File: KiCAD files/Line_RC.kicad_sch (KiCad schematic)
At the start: 56 parts, among them IC1 ESP32-WROVER-E-N4R8, IC2 CP2102N-A02-GQFN28R, IC3 BC847BDW1T1G, IC4 TLV75533PDBVR, IC5 ST1S40IPHR, J1 XT60PW-M, J2 XT60PW-M, J3 Conn_02x02_Odd_Even, J6 Motor OUT, J7 Motor OUT, U1 SL19-121, U3 DRV8213RTER, U4 DRV8213RTER

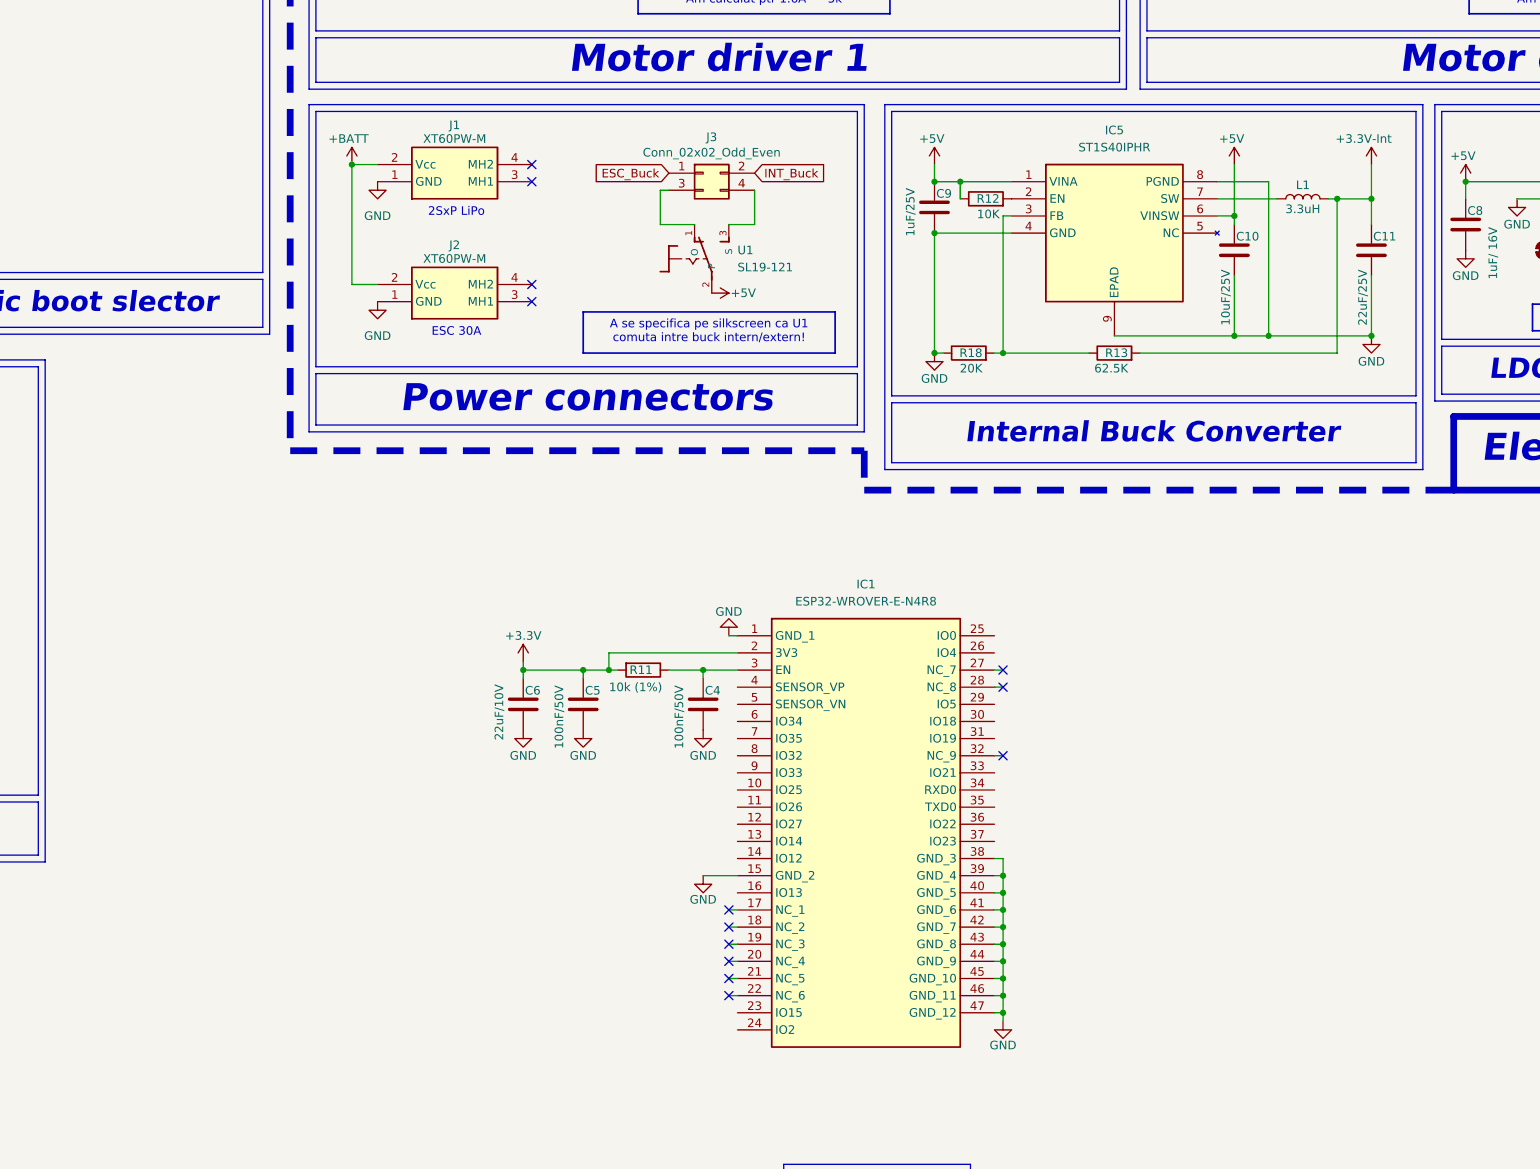
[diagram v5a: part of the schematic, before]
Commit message: Added the connector for the ribbon cable
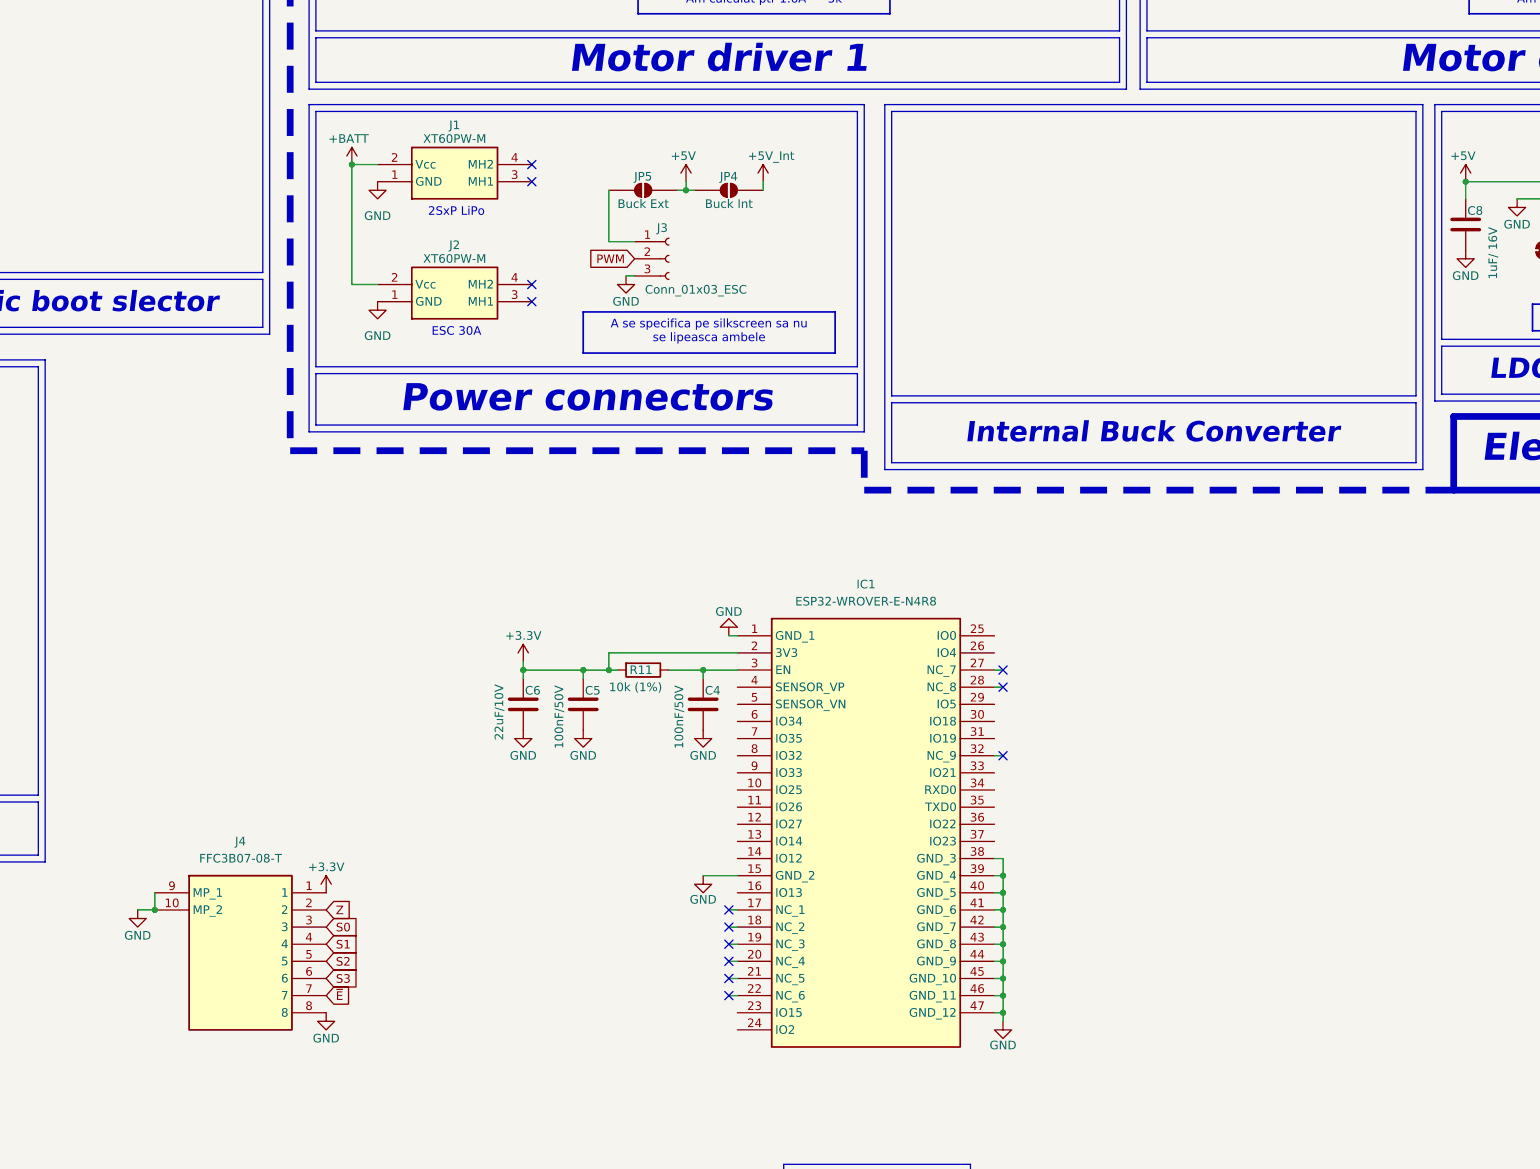
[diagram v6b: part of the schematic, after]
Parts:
- removed C10: 10uF/25V, symbol Device:C
- removed C11: 22uF/25V, symbol Device:C
- removed C9: 1uF/25V, symbol Device:C
- removed IC5: ST1S40IPHR, SOIC127P600X175-9N, symbol ST1S40IPHR:ST1S40IPHR
- removed J3: Conn_02x02_Odd_Even, Connector_PinHeader_1.27mm:PinHeader_2x02_P1.27mm_Vertical, symbol Connector_Generic:Conn_02x02_Odd_Even
- removed L1: 3.3uH, symbol Device:L
- removed R12: 10K, symbol Device:R
- removed R13: 62.5K, symbol Device:R
- removed R18: 20K, symbol Device:R
- removed U1: SL19-121, SL19-121:255SB, symbol SL19-121:SL19-121
- added J3: Conn_01x03_ESC, symbol Connector:Conn_01x03_Socket
- added J4: FFC3B07-08-T, FFC3B0708T, symbol FFC3B07-08-T:FFC3B07-08-T
- added JP4: Buck Int, symbol Jumper:SolderJumper_2_Open
- added JP5: Buck Ext, symbol Jumper:SolderJumper_2_Open
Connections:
- net +3.3V: now also J4.1
- net +5V: now also JP4.1 (A), JP5.2 (B)
- net GND: now also J3.3 (Pin_3), J4.10 (MP_2), J4.8, J4.9 (MP_1)
- new net: J3.1 (Pin_1), JP5.1 (A)
- new net +5V_Int: JP4.2 (B)
- new net PWM: J3.2 (Pin_2)
- new net S0: J4.3
- new net S1: J4.4
- new net S2: J4.5
- new net S3: J4.6
- new net Z: J4.2
- new net ~{E}: J4.7

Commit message: Added TPS Buck IC
Added the TPS563240 Buck IC for the +Batt to 5v conversion before the LDO. The values are taken straight out of the datasheet. Also added different test points across the schematic.
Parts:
- added C10: 100nF, symbol Device:C
- added C11: 22uF, symbol Device:C
- added C12, C9: 10uF, symbol Device:C
- added IC5: TPS563240DDCR, SOT95P280X110-6N, symbol TPS563240DDCR:TPS563240DDCR
- added JP3: 0R, symbol Jumper:SolderJumper_2_Bridged
- added JP6: C4, symbol Jumper:SolderJumper_2_Open
- added L1: 1.5uH, symbol Device:L
- added R12: 73.2k, symbol Device:R
- added R3, R4: 10k, symbol Device:R
- added TP1: 5v_intern, symbol Connector:TestPoint
- added TP2: Batt, symbol Connector:TestPoint
- added TP3: GND, symbol Connector:TestPoint
- added TP4: 5V rail, symbol Connector:TestPoint
- added TP5: PWM, symbol Connector:TestPoint
- added TP6: Vref, symbol Connector:TestPoint
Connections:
- net +3.3V: now also TP6.1
- net +5V: now also TP4.1
- net +5V_Int: now also C11.1, C12.1, JP6.2 (B), L1.1, R12.1, TP1.1
- net +BATT: now also C9.1, IC5.3 (VIN), R3.2, TP2.1
- net GND: now also C11.2, C12.2, C9.2, IC5.1 (GND), R4.1, TP3.1
- net PWM: now also TP5.1
- new net: IC5.5 (EN), R3.1
- new net: C10.1, IC5.2 (SW), L1.2
- new net: IC5.4 (VFB), JP6.1 (A), R12.2, R4.2
- new net: IC5.6 (VBST), JP3.2 (B)
- new net: C10.2, JP3.1 (A)
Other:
- moved on the sheet: C4, C5, C6, IC1, J4, R11

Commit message: added new motor driver
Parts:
- removed C13, C17: 47uF/16V, symbol Device:C
- removed C14, C16, C18, C20: 100nF/50V, symbol Device:C
- removed C15, C19: 22nF/50V, symbol Device:C
- removed J6, J7: Motor OUT, symbol Connector_Generic:Conn_01x02
- removed R14, R16: 10k (1%), symbol Device:R
- removed R15, R17: 5k (1%), symbol Device:R
- removed TP6: Vref, symbol Connector:TestPoint
- removed U3, U4: DRV8213RTER, RTE0016C-IPC_A, symbol 2026-07-26_14-19-18:DRV8213RTER
- added C21, C23: 47uF/16V, symbol Device:C
- added C22, C24: 100nF/50V, symbol Device:C
- added J8, J9: Motor OUT, symbol Connector_Generic:Conn_01x02
- added U1, U2: (no value), symbol RZ7899:RZ7899
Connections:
- net +BATT: now also C21.1, C22.1, C23.1, C24.1, U1.4 (VCC)
- net GND: now also C21.2, C22.2, C23.2, C24.2, U1.3 (GND), U2.3 (GND)
- new net: J9.1 (Pin_1), U2.7 (BO), U2.8 (BO)
- new net: J9.2 (Pin_2), U2.5 (FO), U2.6 (FO)
- new net: J8.1 (Pin_1), U1.7 (BO), U1.8 (BO)
- new net: J8.2 (Pin_2), U1.5 (FO), U1.6 (FO)
- new net A1: U1.2 (FI)
- new net A2: U2.2 (FI)
- new net B1: U1.1 (BI)
- new net B2: U2.1 (BI)
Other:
- note added: "Motor driver 2"
- moved on the sheet: C10, C11, C12, C7, C8, C9, IC4, IC5, J1, J2, J3, JP2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
